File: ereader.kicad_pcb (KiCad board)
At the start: 4 copper layers, 66 x 115 mm, 56 parts, among them J1 USB-C-16P, J2 EPD_FPC_24P, J3 FL_FPC_6P, J4 microSD, J5 Battery_1S, SW1 BTN_A, SW2 BTN_B, SW3 BTN_C, SW4 SLLB510200, U1 ESP32-S3-WROOM-1-N16R8, U2 BQ25628E (PLACEHOLDER-VERIFY), U3 MAX17048 (PLACEHOLDER-VERIFY), U4 LM3630A (PLACEHOLDER-VERIFY), U5 TPS62840 (PLACEHOLDER-VERIFY), U6 USBLC6-2SC6

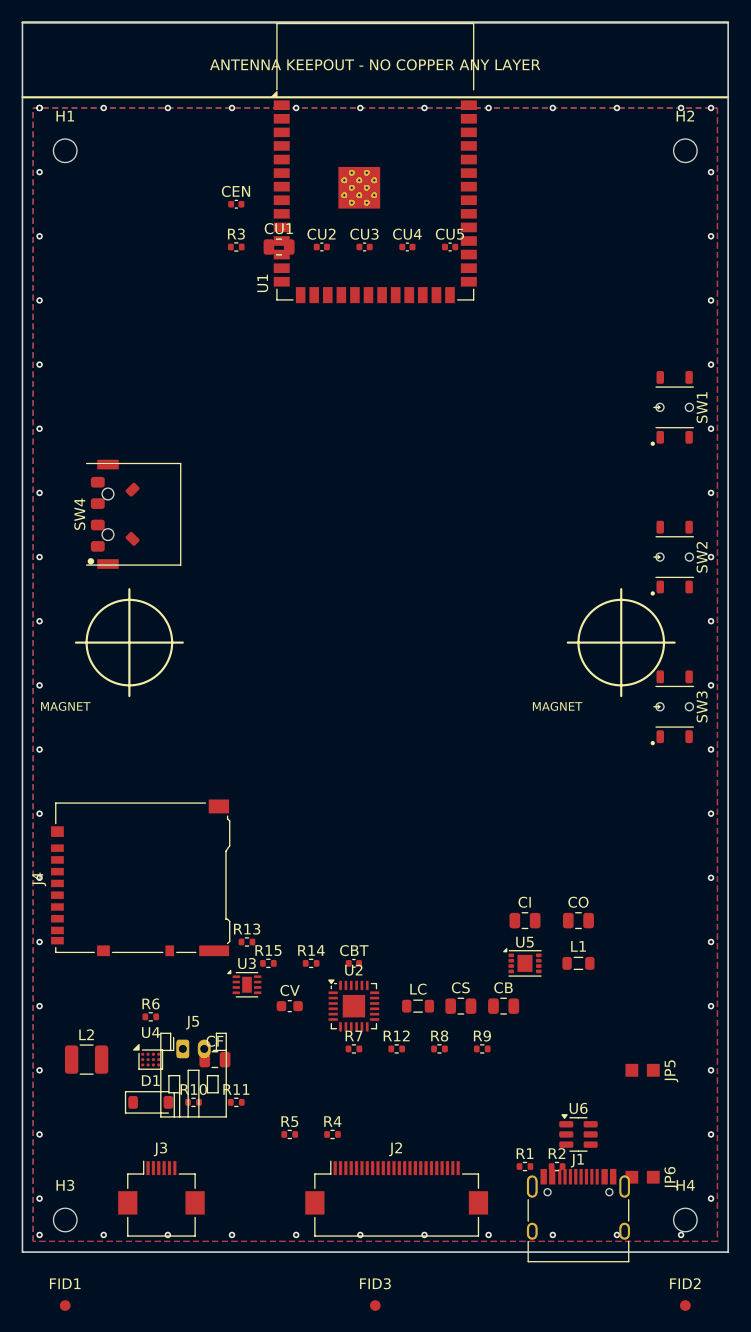
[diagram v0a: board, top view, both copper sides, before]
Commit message: Rearrange crowded components to clear courtyard overlaps
Board is in placement phase (no tracks routed), so footprints move freely.
Resolves every same-side courtyard overlap flagged in the placement review
(verified 0 overlaps remaining). No vias coincide with any moved part, so
none had to travel; copper zones refill automatically.

ESP32 (U1) decoupling — out from under the module body / antenna keep-out
into a row just below the module:
  CEN 20,17->18,29  CU1 24,21->22,29  CU2 28,21->26,29  CU3 32,21->30,29
  CU4 36,21->34,29  CU5 40,21->38,29  R3 20,21->42,29

Battery/charger cluster — spread out of the JST J5 courtyard (body + cable
clearance) to the right of the connector:
  U4 12,97->22,99.5  CF 18,97->26.5,102  D1 12,101->30,99.5
  R10 16,101->23.5,102.6  R11 20,101->29.5,102.5

USB-C (J1) — de-conflicted from the connector courtyard:
  JP6 58,108->58,103  R1 47,107->45.4,108  R2 50,107->45.4,111

Only rotations preserved; positions are the sole change. Two sub-0.3mm
pairs (R13/J4, R15/U3) already pass courtyard DRC and were left as-is.

Co-Authored-By: Claude Opus 4.8 <noreply@anthropic.com>
Claude-Session: https://claude.ai/code/session_01URcq3obYmoK54WE6UNQt7F
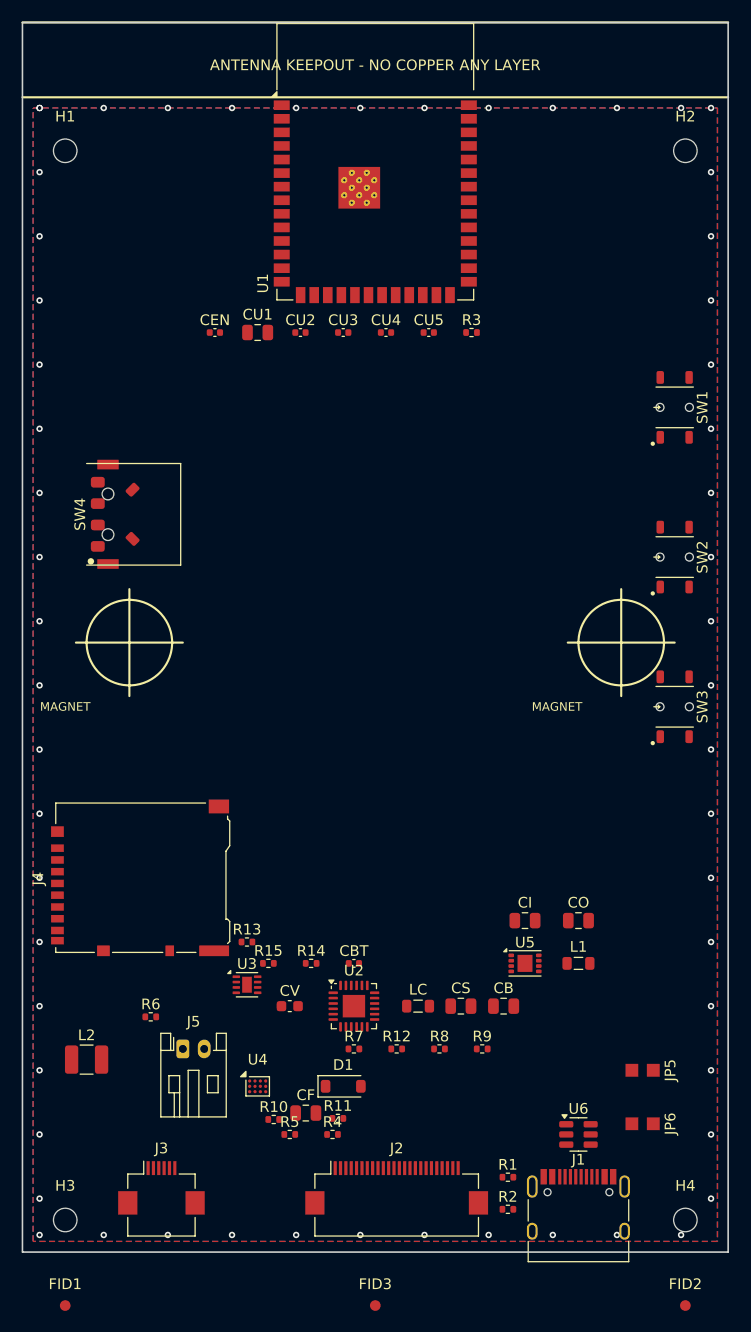
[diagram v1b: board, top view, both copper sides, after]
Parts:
- moved R3 23.4 mm to (42.0, 29.0)
- moved D1 18.1 mm to (30.0, 99.5)
- moved CEN 12.2 mm to (18.0, 29.0)
- moved U4 10.3 mm to (22.0, 99.5)
- moved CF 9.86 mm to (26.5, 102.0)
- moved R11 9.62 mm to (29.5, 102.5)
- moved CU1 8.25 mm to (22.0, 29.0)
- moved CU2 8.25 mm to (26.0, 29.0)
- moved CU3 8.25 mm to (30.0, 29.0)
- moved CU4 8.25 mm to (34.0, 29.0)
- moved CU5 8.25 mm to (38.0, 29.0)
- moved R10 7.67 mm to (23.5, 102.6)
- moved R2 6.10 mm to (45.4, 111.0)
- moved JP6 5.00 mm to (58.0, 103.0)
- moved R1 1.89 mm to (45.4, 108.0)
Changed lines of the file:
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@@
   )
   (footprint "C_0805_2012Metric" (layer "F.Cu")
-    (at 18 97)
+    (at 26.5 102)
     (descr "Capacitor SMD 0805 (2012 Metric), square (rectangular) end terminal, IPC_7351 nominal, (Body size source: IPC-SM-782 page 76, https://www.pcb-3d.com/wordpress/wp-content/uploads/ipc-sm-782a_amendment_1_and_2.pdf, https://docs.google.com/spreadsheets/d/1BsfQQcO9C6DZCsRaXUlFlo91Tg2WpOkGARC1WS5S8t0/edit?usp=sharing), generated with kicad-footprint-generator")
     (tags "capacitor")
@@
   )
   (footprint "R_0402_1005Metric" (layer "F.Cu")
-    (at 16 101)
+    (at 23.5 102.6)
     (descr "Resistor SMD 0402 (1005 Metric), square (rectangular) end terminal, IPC_7351 nominal, (Body size source: IPC-SM-782 page 72, https://www.pcb-3d.com/wordpress/wp-content/uploads/ipc-sm-782a_amendment_1_and_2.pdf), generated with kicad-footprint-generator")
     (tags "resistor")
@@
   )
   (footprint "R_0402_1005Metric" (layer "F.Cu")
-    (at 50 107)
+    (at 45.4 111)
     (descr "Resistor SMD 0402 (1005 Metric), square (rectangular) end terminal, IPC_7351 nominal, (Body size source: IPC-SM-782 page 72, https://www.pcb-3d.com/wordpress/wp-content/uploads/ipc-sm-782a_amendment_1_and_2.pdf), generated with kicad-footprint-generator")
     (tags "resistor")
@@
   )
   (footprint "C_0402_1005Metric" (layer "F.Cu")
-    (at 36 21)
+    (at 34 29)
     (descr "Capacitor SMD 0402 (1005 Metric), square (rectangular) end terminal, IPC_7351 nominal, (Body size source: IPC-SM-782 page 76, https://www.pcb-3d.com/wordpress/wp-content/uploads/ipc-sm-782a_amendment_1_and_2.pdf), generated with kicad-footprint-generator")
     (tags "capacitor")
@@
   )
   (footprint "R_0402_1005Metric" (layer "F.Cu")
-    (at 20 101)
+    (at 29.5 102.5)
     (descr "Resistor SMD 0402 (1005 Metric), square (rectangular) end terminal, IPC_7351 nominal, (Body size source: IPC-SM-782 page 72, https://www.pcb-3d.com/wordpress/wp-content/uploads/ipc-sm-782a_amendment_1_and_2.pdf), generated with kicad-footprint-generator")
     (tags "resistor")
@@
   )
   (footprint "C_0402_1005Metric" (layer "F.Cu")
-    (at 28 21)
+    (at 26 29)
     (descr "Capacitor SMD 0402 (1005 Metric), square (rectangular) end terminal, IPC_7351 nominal, (Body size source: IPC-SM-782 page 76, https://www.pcb-3d.com/wordpress/wp-content/uploads/ipc-sm-782a_amendment_1_and_2.pdf), generated with kicad-footprint-generator")
     (tags "capacitor")
@@
   )
   (footprint "ereader:JumperPad_2P_P2.0mm" (layer "F.Cu")
-    (at 58 108 270)
+    (at 58 103 270)
     (descr "Bare 2-pad exposed jumper (no switch part) - momentarily short with a screwdriver tip or tweezers to pull EN low for RESET. Open circuit in normal use.")
     (tags "jumper test pad reset bare pads screwdriver")
@@
   )
   (footprint "D_SOD-123" (layer "F.Cu")
-    (at 12 101)
+    (at 30 99.5)
     (descr "SOD-123")
     (tags "SOD-123")
@@
   )
   (footprint "C_0402_1005Metric" (layer "F.Cu")
-    (at 32 21)
+    (at 30 29)
     (descr "Capacitor SMD 0402 (1005 Metric), square (rectangular) end terminal, IPC_7351 nominal, (Body size source: IPC-SM-782 page 76, https://www.pcb-3d.com/wordpress/wp-content/uploads/ipc-sm-782a_amendment_1_and_2.pdf), generated with kicad-footprint-generator")
     (tags "capacitor")
@@
   )
   (footprint "C_0402_1005Metric" (layer "F.Cu")
-    (at 40 21)
+    (at 38 29)
     (descr "Capacitor SMD 0402 (1005 Metric), square (rectangular) end terminal, IPC_7351 nominal, (Body size source: IPC-SM-782 page 76, https://www.pcb-3d.com/wordpress/wp-content/uploads/ipc-sm-782a_amendment_1_and_2.pdf), generated with kicad-footprint-generator")
     (tags "capacitor")
@@
   )
   (footprint "C_0805_2012Metric" (layer "F.Cu")
-    (at 24 21)
+    (at 22 29)
     (descr "Capacitor SMD 0805 (2012 Metric), square (rectangular) end terminal, IPC_7351 nominal, (Body size source: IPC-SM-782 page 76, https://www.pcb-3d.com/wordpress/wp-content/uploads/ipc-sm-782a_amendment_1_and_2.pdf, https://docs.google.com/spreadsheets/d/1BsfQQcO9C6DZCsRaXUlFlo91Tg2WpOkGARC1WS5S8t0/edit?usp=sharing), generated with kicad-footprint-generator")
     (tags "capacitor")
@@
   )
   (footprint "C_0402_1005Metric" (layer "F.Cu")
-    (at 20 17)
+    (at 18 29)
     (descr "Capacitor SMD 0402 (1005 Metric), square (rectangular) end terminal, IPC_7351 nominal, (Body size source: IPC-SM-782 page 76, https://www.pcb-3d.com/wordpress/wp-content/uploads/ipc-sm-782a_amendment_1_and_2.pdf), generated with kicad-footprint-generator")
     (tags "capacitor")
@@
   )
   (footprint "R_0402_1005Metric" (layer "F.Cu")
-    (at 47 107)
+    (at 45.4 108)
     (descr "Resistor SMD 0402 (1005 Metric), square (rectangular) end terminal, IPC_7351 nominal, (Body size source: IPC-SM-782 page 72, https://www.pcb-3d.com/wordpress/wp-content/uploads/ipc-sm-782a_amendment_1_and_2.pdf), generated with kicad-footprint-generator")
     (tags "resistor")
@@
   )
   (footprint "R_0402_1005Metric" (layer "F.Cu")
-    (at 20 21)
+    (at 42 29)
     (descr "Resistor SMD 0402 (1005 Metric), square (rectangular) end terminal, IPC_7351 nominal, (Body size source: IPC-SM-782 page 72, https://www.pcb-3d.com/wordpress/wp-content/uploads/ipc-sm-782a_amendment_1_and_2.pdf), generated with kicad-footprint-generator")
     (tags "resistor")
@@
   )
   (footprint "Maxim_WLP-12" (layer "F.Cu")
-    (at 12 97)
+    (at 22 99.5)
     (descr "Maxim_WLP-12 W121B2+1 http://pdfserv.maximintegrated.com/package_dwgs/21-0009.PDF")
     (tags "Maxim_WLP-12")

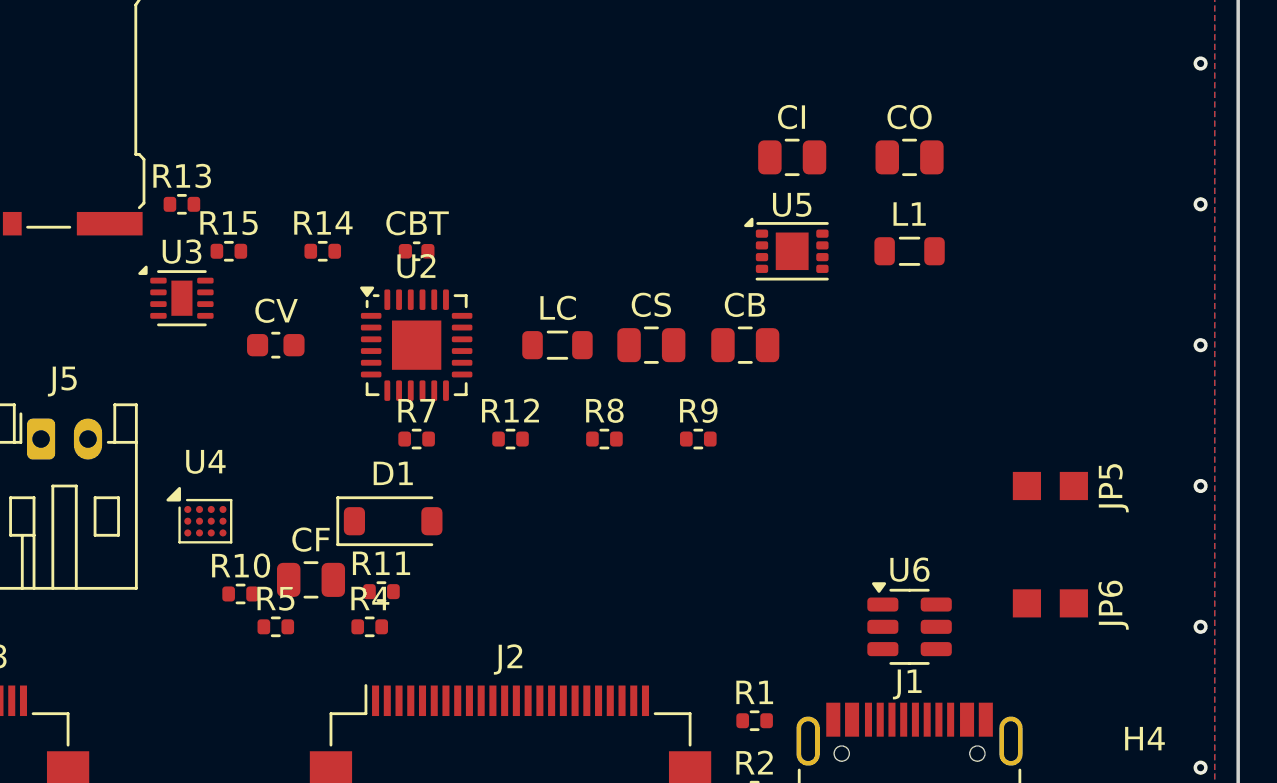
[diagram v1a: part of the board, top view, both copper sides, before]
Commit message: Clear last tight clearances and tidy moved-part silkscreen refs
Tighten the two sub-0.3mm pairs left by the previous rearrange (now >=0.4mm
courtyard clearance), verified 0 overlaps / 0 tight remaining:
  R13 21,86 -> 22,85.5   (was 0.25mm to J4 microSD)
  R15 23,88 -> 23.5,87.3 (was 0.28mm to U3)

Tidy reference-designator silkscreen for moved parts so no ref text overlaps
a pad, another ref, or a component body (verified 0 ref clashes):
  R10 ref offset -> left of part      R11 ref offset -> right of part
  JP6 ref offset -> clear of J1/U6    R15 ref centered on its own pad
     (only clear spot in the R13/U3/R14 pocket; clears all neighbours 0.25mm)
Reference text only; component positions unchanged except the two nudges.

Co-Authored-By: Claude Opus 4.8 <noreply@anthropic.com>
Claude-Session: https://claude.ai/code/session_01URcq3obYmoK54WE6UNQt7F
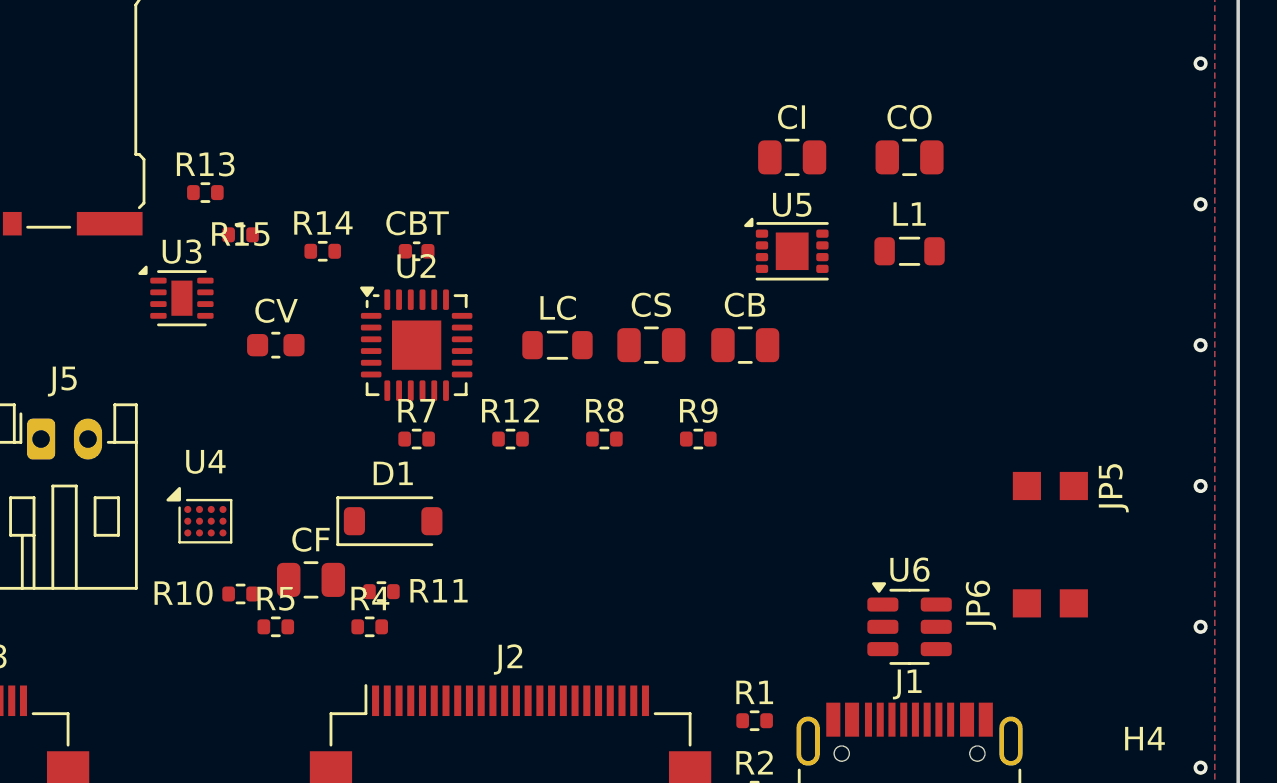
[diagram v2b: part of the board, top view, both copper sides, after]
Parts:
- moved R13 1.12 mm to (22.0, 85.5)
- moved R15 0.86 mm to (23.5, 87.3)
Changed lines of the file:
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@@
   )
   (footprint "R_0402_1005Metric" (layer "F.Cu")
-    (at 23 88)
+    (at 23.5 87.3)
     (descr "Resistor SMD 0402 (1005 Metric), square (rectangular) end terminal, IPC_7351 nominal, (Body size source: IPC-SM-782 page 72, https://www.pcb-3d.com/wordpress/wp-content/uploads/ipc-sm-782a_amendment_1_and_2.pdf), generated with kicad-footprint-generator")
     (tags "resistor")
     (attr smd)
-    (fp_text reference "R15" (at 0 -1.17) (layer "F.SilkS")
+    (fp_text reference "R15" (at 0.0 0.0) (layer "F.SilkS")
         (effects (font (size 1 1) (thickness 0.15)))
     )
@@
     (tags "resistor")
     (attr smd)
-    (fp_text reference "R10" (at 0 -1.17) (layer "F.SilkS")
+    (fp_text reference "R10" (at -2.45 0) (layer "F.SilkS")
         (effects (font (size 1 1) (thickness 0.15)))
     )
@@
   )
   (footprint "R_0402_1005Metric" (layer "F.Cu")
-    (at 21 86)
+    (at 22 85.5)
     (descr "Resistor SMD 0402 (1005 Metric), square (rectangular) end terminal, IPC_7351 nominal, (Body size source: IPC-SM-782 page 72, https://www.pcb-3d.com/wordpress/wp-content/uploads/ipc-sm-782a_amendment_1_and_2.pdf), generated with kicad-footprint-generator")
     (tags "resistor")
@@
     (tags "resistor")
     (attr smd)
-    (fp_text reference "R11" (at 0 -1.17) (layer "F.SilkS")
+    (fp_text reference "R11" (at 2.45 0) (layer "F.SilkS")
         (effects (font (size 1 1) (thickness 0.15)))
     )
@@
     (tags "jumper test pad reset bare pads screwdriver")
     (attr smd)
-    (fp_text reference "JP6" (at 0 -2.6 270) (layer "F.SilkS")
-        (effects (font (size 1 1) (thickness 0.15)))
-    )
+    (fp_text reference "JP6" (at 0 3.05 270) (layer "F.SilkS")
+        (effects (font (size 1 1) (thickness 0.15)))
+    )
